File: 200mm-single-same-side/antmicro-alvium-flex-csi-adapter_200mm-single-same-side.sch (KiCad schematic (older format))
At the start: 2 parts, among them J1 WE_687622100002_FLEX, J2 WE_687650100002_FLEX

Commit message: 200mm-single-same: update signage
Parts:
- added N1: oshw_logo, antmicro-alvium-flex-csi-adapter-footprints:oshw-logo, symbol antmicro-alvium-flex-csi-adapter:oshw_logo
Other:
- note added: "Alvium Camera"
- note added: "Alvium flex CSI adapter 200mm single same side contacts"
- note added: "Antmicro CSI interface"
- note removed: "Antmicro - Alvium Flex CSI Adapter"
- note removed: "FFC contacts - Alvium side"
- note removed: "FFC contacts - Antmicro side"
- moved on the sheet: J1, J2

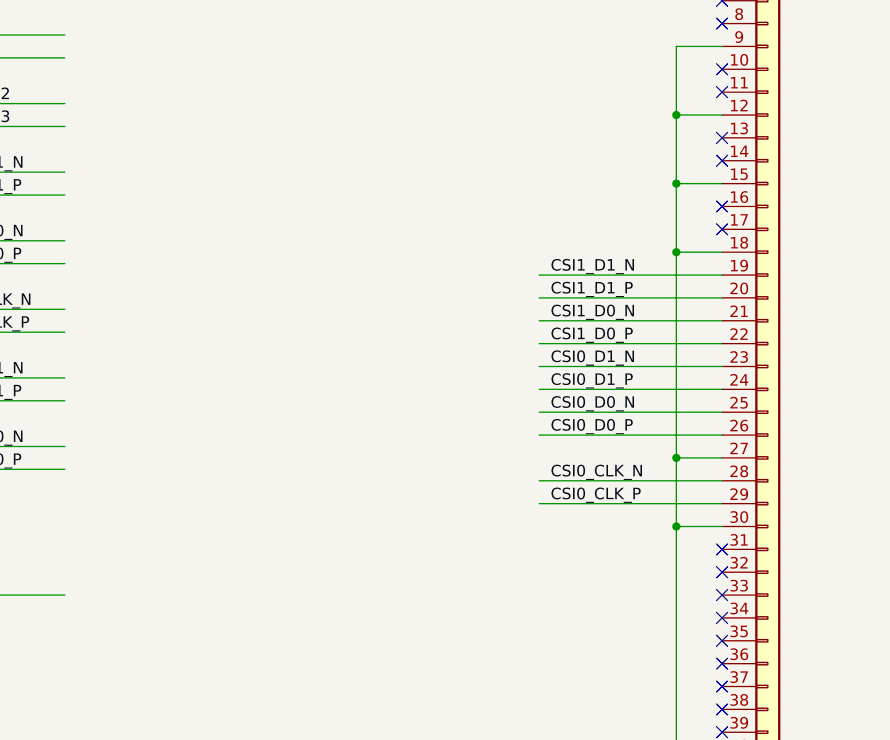
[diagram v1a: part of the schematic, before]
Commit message: 200mm-single-same: add NMOS transistor for camera triggering
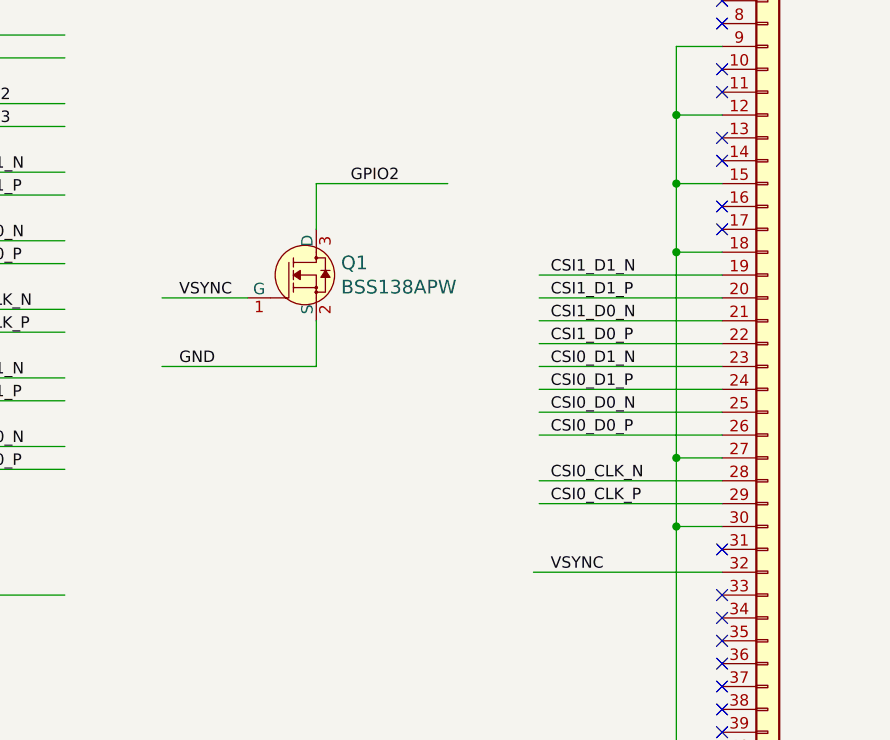
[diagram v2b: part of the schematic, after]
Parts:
- added Q1: BSS138APW, antmicro-alvium-flex-csi-adapter-footprints:SC70-3, symbol antmicro-alvium-flex-csi-adapter:BSS138APW
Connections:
- net labels added: VSYNC
- wire segments 61 -> 67
- no-connect marks 30 -> 29
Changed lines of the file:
@@
 Text Notes 6075 3150 0    79   ~ 16
 Alvium Camera
-NoConn ~ 10100 6425
 Text Notes 9775 3050 0    79   ~ 16
 Antmicro CSI interface
@@
 	1    0    0    -1
 $EndComp
+Wire Wire Line
+	10100 6425 9275 6425
+Text Label 9350 6425 0    50   ~ 0
+VSYNC
+Text Label 7725 5225 0    50   ~ 0
+VSYNC
+Text Label 8475 4725 0    50   ~ 0
+GPIO2
+Text Label 7725 5525 0    50   ~ 0
+GND
+$Comp
+L antmicro-alvium-flex-csi-adapter:BSS138APW Q1
+U 1 1 5F8886C3
+P 8325 5125
+F 0 "Q1" H 8433 5178 60  0000 L CNN
+F 1 "BSS138APW" H 8433 5072 60  0000 L CNN
+F 2 "antmicro-alvium-flex-csi-adapter-footprints:SC70-3" H 8525 5325 60  0001 L CNN
+F 3 "" H 8525 5425 60  0001 L CNN
+F 4 "BSS138PW" H 8525 5625 60  0001 L CNN "MPN"
+F 5 "ON Semiconductor" H 8525 6225 60  0001 L CNN "Manufacturer"
+	1    8325 5125
+	1    0    0    -1
+$EndComp
+Wire Wire Line
+	8325 5325 8325 5525
+Wire Wire Line
+	8325 5525 7650 5525
+Wire Wire Line
+	8025 5225 7650 5225
+Wire Wire Line
+	8325 4925 8325 4725
+Wire Wire Line
+	8325 4725 8900 4725
 $EndSCHEMATC
